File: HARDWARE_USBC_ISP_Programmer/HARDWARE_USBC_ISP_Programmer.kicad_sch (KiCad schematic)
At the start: 45 parts

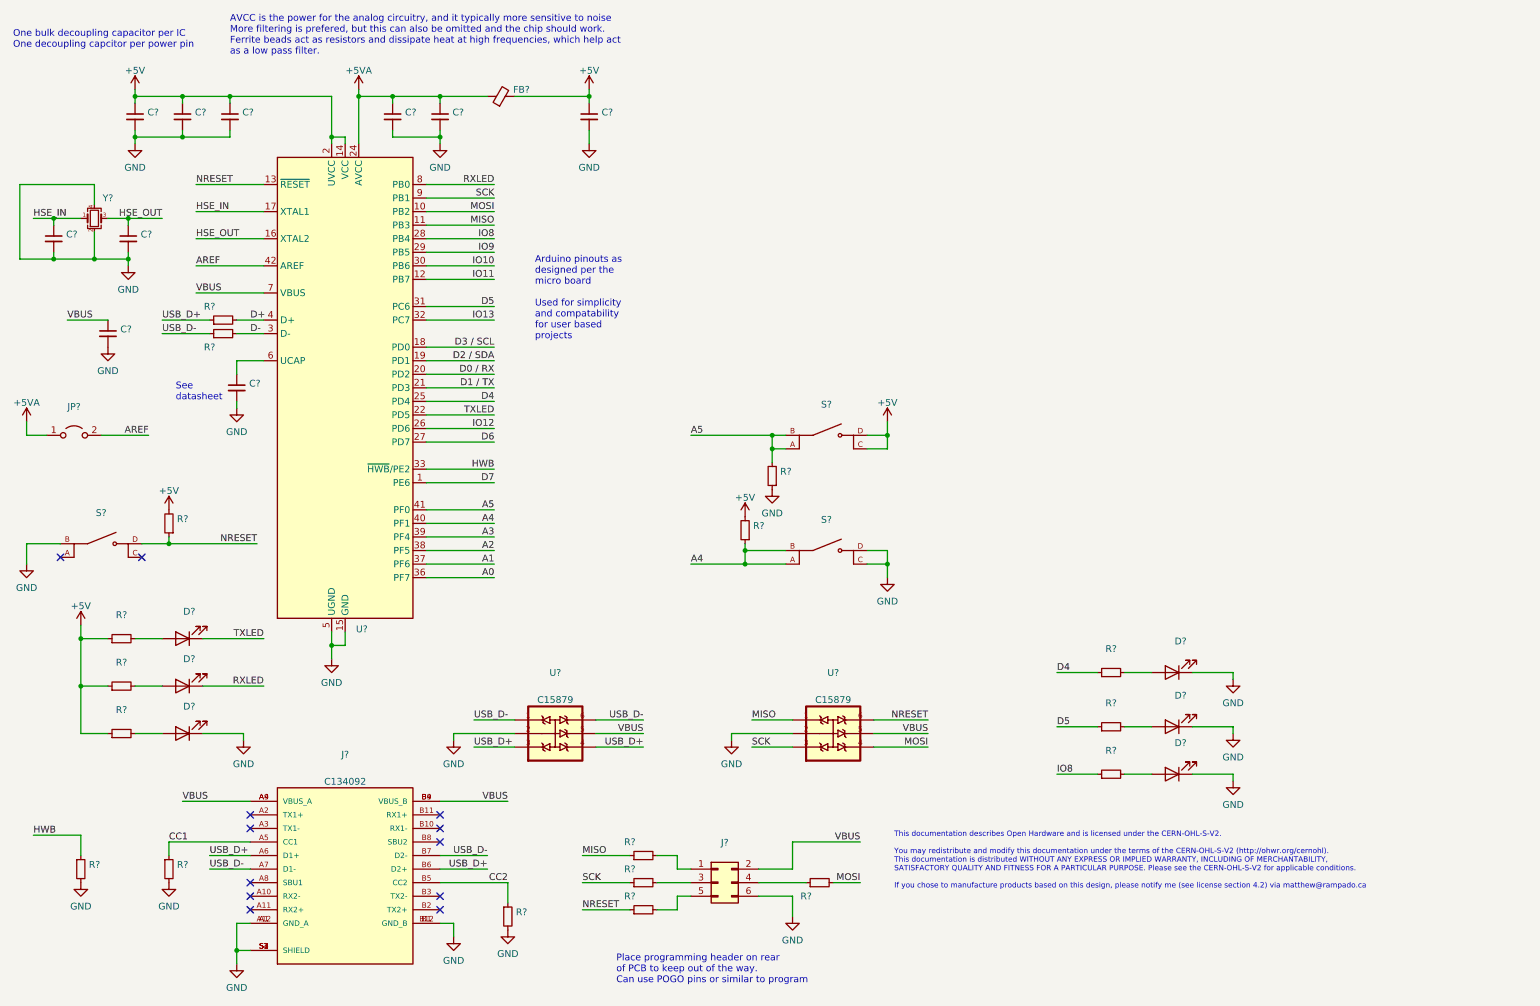
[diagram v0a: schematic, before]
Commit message: Added headers to schematic, other minor changes
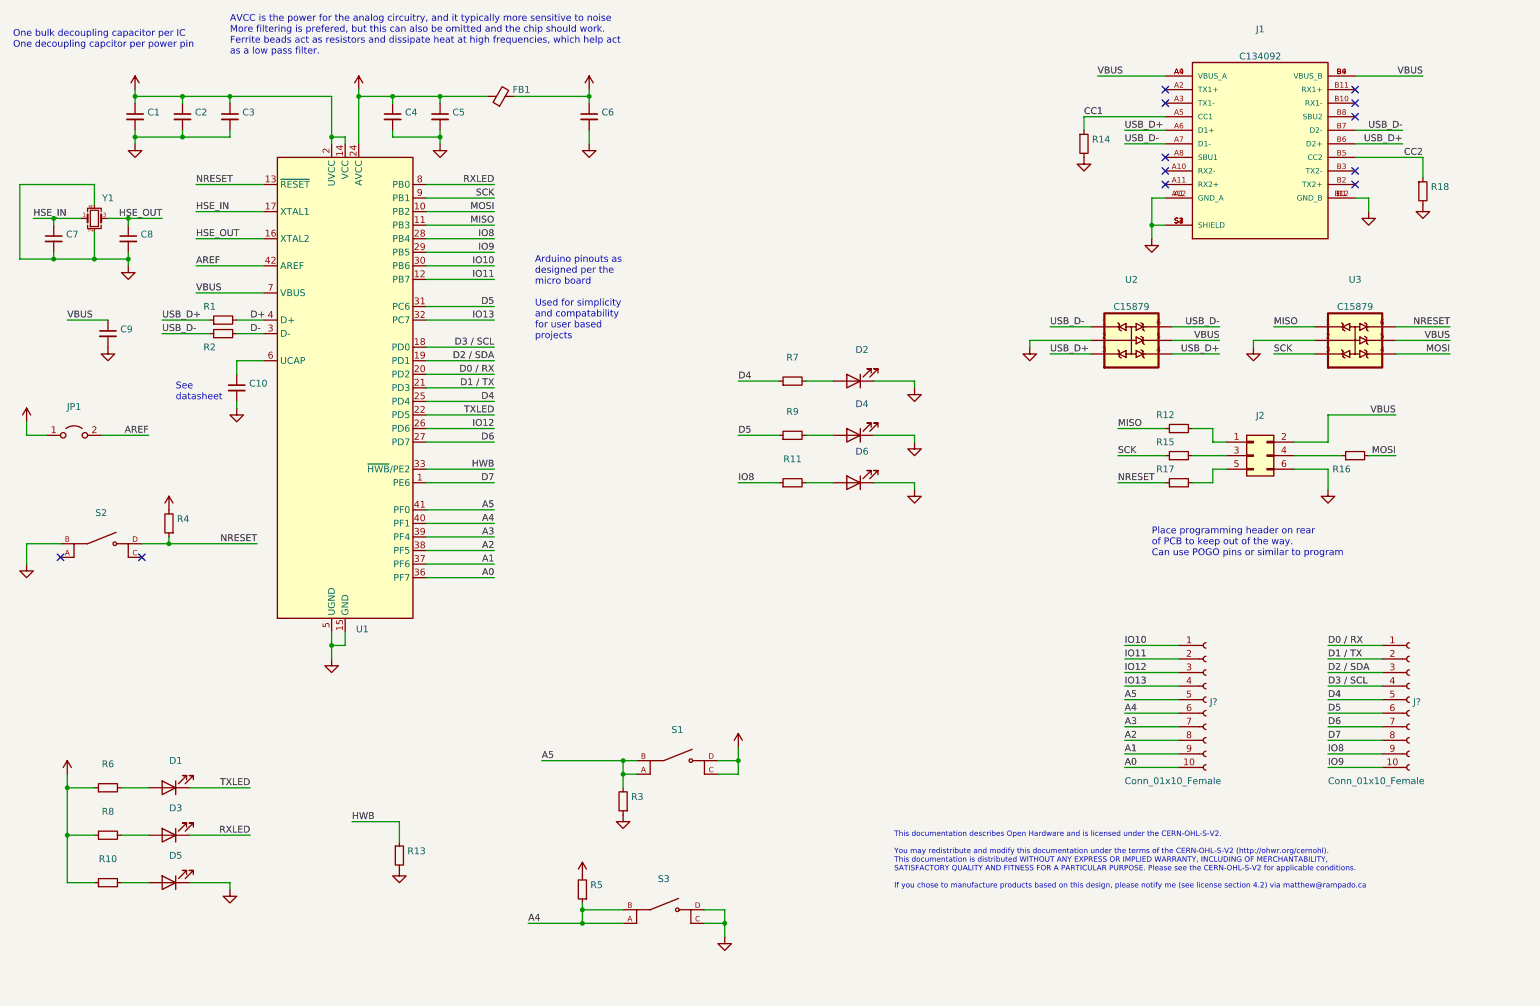
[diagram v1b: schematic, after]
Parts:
- added J? (x2): Conn_01x10_Female, symbol Connector:Conn_01x10_Female
- J1: renamed from J?; footprint (none) -> Rampado_Master:MOLEX_105450-0101
- S1, S2, S3: renamed from S?; footprint (none) -> Rampado_Master:SW_TS-1187A-B-A-B
- U2, U3: renamed from U?; footprint (none) -> Rampado_Master:SOT65P210X110-6N
- gave numbers to parts that had none: 39
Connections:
- net A0: now also J?.10 (Pin_10)
- net A1: now also J?.9 (Pin_9)
- net A2: now also J?.8 (Pin_8)
- net A3: now also J?.7 (Pin_7)
- net A4: now also J?.6 (Pin_6)
- net A5: now also J?.5 (Pin_5)
- net D0 / RX: now also J?.1 (Pin_1)
- net D1 / TX: now also J?.2 (Pin_2)
- net D2 / SDA: now also J?.3 (Pin_3)
- net D3 / SCL: now also J?.4 (Pin_4)
- net D4: now also J?.5 (Pin_5)
- net D5: now also J?.6 (Pin_6)
- net D6: now also J?.7 (Pin_7)
- net D7: now also J?.8 (Pin_8)
- net IO10: now also J?.1 (Pin_1)
- net IO11: now also J?.2 (Pin_2)
- net IO12: now also J?.3 (Pin_3)
- net IO13: now also J?.4 (Pin_4)
- net IO8: now also J?.9 (Pin_9)
- net IO9: now also J?.10 (Pin_10)
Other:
- moved on the sheet: D1, D2, D3, D4, D5, D6, J1, J2, R10, R11, R12, R13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

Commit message: Finalized footprints and schematic
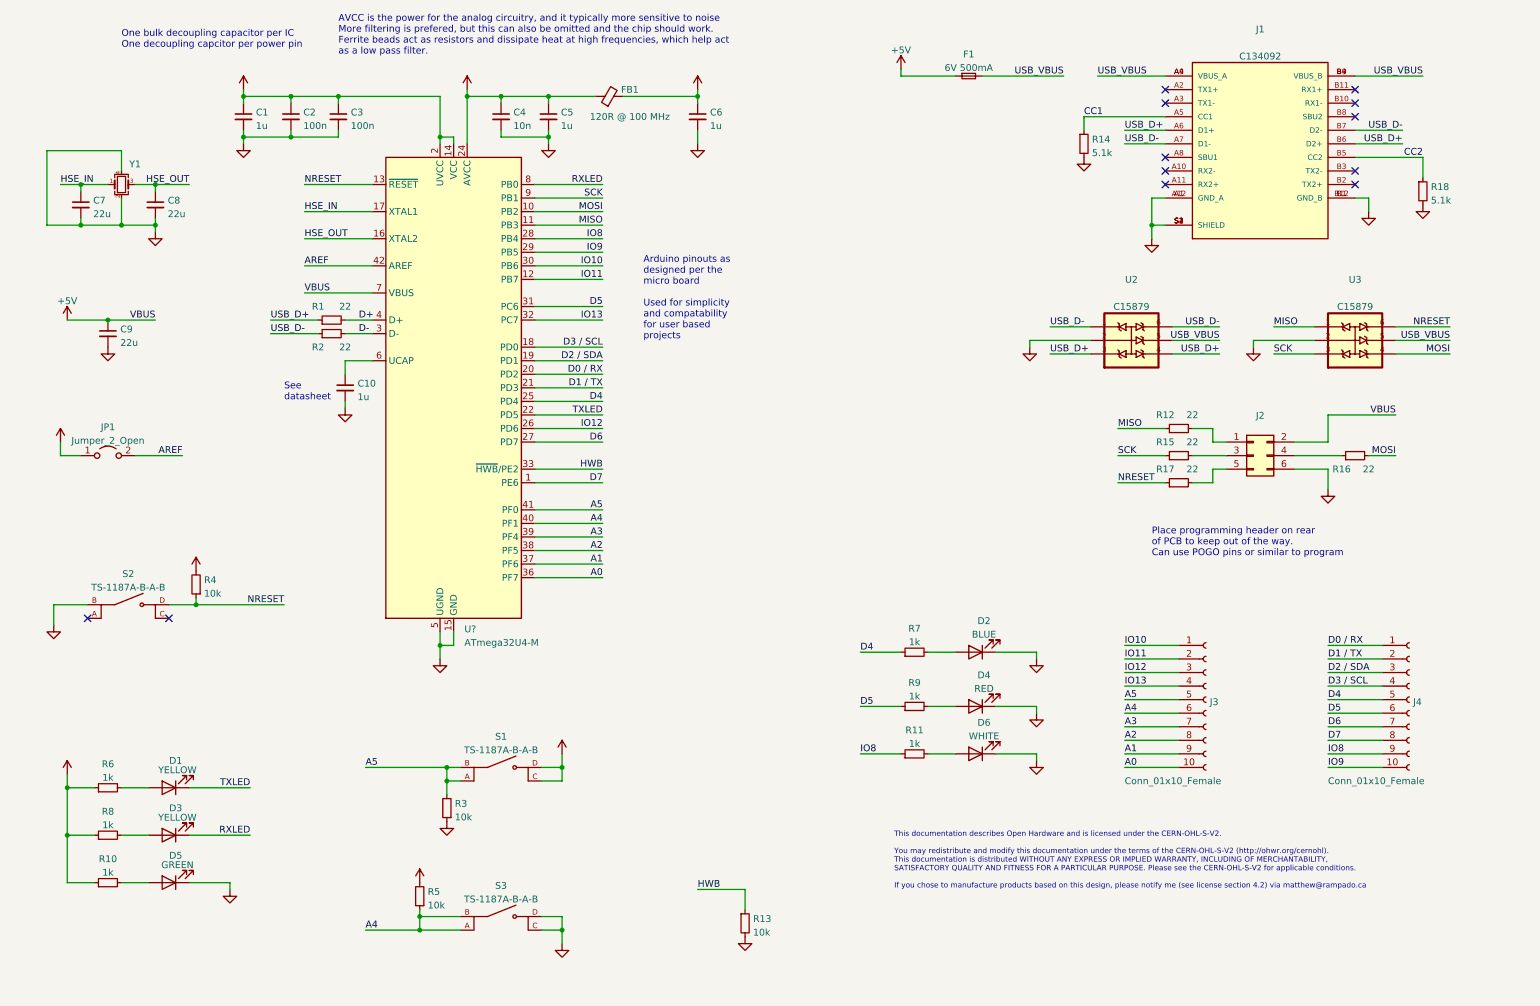
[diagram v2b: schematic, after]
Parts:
- removed U1: (no value), symbol MCU_Microchip_ATmega:ATmega32U4-M
- added F1: 6V 500mA, Fuse:Fuse_0603_1608Metric_Pad1.05x0.95mm_HandSolder, symbol Device:Fuse_Small
- added U?: ATmega32U4-M, Package_DFN_QFN:QFN-44-1EP_7x7mm_P0.5mm_EP5.2x5.2mm, symbol MCU_Microchip_ATmega:ATmega32U4-M
- C1, C10, C5, C6: value (none) -> 1u; footprint (none) -> Capacitor_SMD:C_0603_1608Metric
- C2, C3: value (none) -> 100n; footprint (none) -> Capacitor_SMD:C_0603_1608Metric
- C4: value (none) -> 10n; footprint (none) -> Capacitor_SMD:C_0603_1608Metric
- C7, C8, C9: value (none) -> 22u; footprint (none) -> Capacitor_SMD:C_0603_1608Metric
- D1, D3: value (none) -> YELLOW; footprint (none) -> LED_SMD:LED_0603_1608Metric
- D2: value (none) -> BLUE; footprint (none) -> LED_SMD:LED_0603_1608Metric
- D4: value (none) -> RED; footprint (none) -> LED_SMD:LED_0603_1608Metric
- D5: value (none) -> GREEN; footprint (none) -> LED_SMD:LED_0603_1608Metric
- D6: value (none) -> WHITE; footprint (none) -> LED_SMD:LED_0603_1608Metric
- FB1: value (none) -> 120R @ 100 MHz; footprint (none) -> Inductor_SMD:L_0603_1608Metric
- J2: footprint (none) -> Connector_PinHeader_2.54mm:PinHeader_2x03_P2.54mm_Vertical
- J3, J4: renamed from J?; footprint (none) -> Connector_PinSocket_2.54mm:PinSocket_1x10_P2.54mm_Vertical
- JP1: value (none) -> Jumper_2_Open; footprint (none) -> Jumper:SolderJumper-2_P1.3mm_Open_RoundedPad1.0x1.5mm
- R1, R12, R15, R16, R17, R2: value (none) -> 22; footprint (none) -> Resistor_SMD:R_0603_1608Metric
- R10, R11, R6, R7, R8, R9: value (none) -> 1k; footprint (none) -> Resistor_SMD:R_0603_1608Metric
- R13: value (none) -> 10k; footprint (none) -> Resistor_SMD:R_0603_1608Metric; JLCPCB Part # C23186 -> C25804
- R14, R18: value (none) -> 5.1k; footprint (none) -> Resistor_SMD:R_0603_1608Metric
- R3, R4, R5: value (none) -> 10k; footprint (none) -> Resistor_SMD:R_0603_1608Metric; JLCPCB Part # C21190 -> C25804
- S1, S2, S3: value (none) -> TS-1187A-B-A-B
- Y1: footprint (none) -> Crystal:Crystal_SMD_3225-4Pin_3.2x2.5mm
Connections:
- net +5V: now also C9.1, J2.2 (Pin_2), F1.1, U?.14 (VCC), U?.2 (UVCC), U?.34 (VCC), U?.7 (VBUS)
- net +5VA: now also U?.24 (AVCC), U?.44 (AVCC)
- net A0: now also U?.36 (PF7)
- net A1: now also U?.37 (PF6)
- net A2: now also U?.38 (PF5)
- net A3: now also U?.39 (PF4)
- net A4: now also U?.40 (PF1)
- net A5: now also U?.41 (PF0)
- net AREF: now also U?.42 (AREF)
- net D+: now also U?.4 (D+)
- net D-: now also U?.3 (D-)
- net D0 / RX: now also U?.20 (PD2)
- net D1 / TX: now also U?.21 (PD3)
- net D2 / SDA: now also U?.19 (PD1)
- net D3 / SCL: now also U?.18 (PD0)
- net D4: now also U?.25 (PD4)
- net D5: now also U?.31 (PC6)
- net D6: now also U?.27 (PD7)
- net D7: now also U?.1 (PE6)
- net GND: now also U?.15 (GND), U?.23 (GND), U?.35 (GND), U?.43 (GND), U?.45 (GND), U?.5 (UGND)
- net HSE_IN: now also U?.17 (XTAL1)
- net HSE_OUT: now also U?.16 (XTAL2)
- net HWB: now also U?.33 (~{HWB}/PE2)
- net IO10: now also U?.30 (PB6)
- net IO11: now also U?.12 (PB7)
- net IO12: now also U?.26 (PD6)
- net IO13: now also U?.32 (PC7)
- net IO8: now also U?.28 (PB4)
- net IO9: now also U?.29 (PB5)
- net MISO: now also U?.11 (PB3)
- net MOSI: now also U?.10 (PB2)
- net NRESET: now also U?.13 (~{RESET})
- net RXLED: now also U?.8 (PB0)
- net SCK: now also U?.9 (PB1)
- net TXLED: now also U?.22 (PD5)
- net at C10.1: now also U?.6 (UCAP)
- net VBUS renamed USB_VBUS
- net USB_VBUS: now also F1.2; no longer C9.1, J2.2 (Pin_2)
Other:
- moved on the sheet: C1, C10, C2, C3, C4, C5, C6, C7, C8, D2, D4, D6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

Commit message: Initial PCB layout complete
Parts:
- gave numbers to parts that had none: 1
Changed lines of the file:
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@@
   (symbol (lib_id "MCU_Microchip_ATmega:ATmega32U4-M") (at 95.25 83.82 0) (unit 1)
     (in_bom yes) (on_board yes) (fields_autoplaced)
-    (property "Reference" "U?" (id 0) (at 97.2694 129.0304 0)
+    (property "Reference" "U1" (id 0) (at 97.2694 129.0304 0)
       (effects (font (size 1.27 1.27)) (justify left))
     )
@@
       (reference "S3") (unit 1) (value "TS-1187A-B-A-B") (footprint "Rampado_Master:SW_TS-1187A-B-A-B")
     )
+    (path "/9f43d1c3-9884-48c3-9a0e-a3ae0b6b2875"
+      (reference "U1") (unit 1) (value "ATmega32U4-M") (footprint "Package_DFN_QFN:QFN-44-1EP_7x7mm_P0.5mm_EP5.2x5.2mm")
+    )
     (path "/9d4d08dc-598c-409d-8f88-24678d093d71"
       (reference "U2") (unit 1) (value "SMF05CT1G") (footprint "Rampado_Master:SOT65P210X110-6N")
@@
       (reference "U3") (unit 1) (value "SMF05CT1G") (footprint "Rampado_Master:SOT65P210X110-6N")
     )
-    (path "/9f43d1c3-9884-48c3-9a0e-a3ae0b6b2875"
-      (reference "U?") (unit 1) (value "ATmega32U4-M") (footprint "Package_DFN_QFN:QFN-44-1EP_7x7mm_P0.5mm_EP5.2x5.2mm")
-    )
     (path "/ad3562f5-456c-4345-9674-ab2e13f88574"

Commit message: V1 routing complete
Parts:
- J1: value (none) -> 105450-0101
- J2: value (none) -> Conn_02x03_Odd_Even
- U2, U3: value (none) -> SMF05CT1G
- Y1: value (none) -> 16MHz
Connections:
- net +5V: now also U3.5
- net USB_VBUS: no longer U3.5
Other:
- moved on the sheet: U2, U3

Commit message: Created manufacturing files and prepare for review
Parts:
- FB1: footprint Inductor_SMD:L_0603_1608Metric -> Inductor_SMD:L_0805_2012Metric
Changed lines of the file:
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@@
   (symbol (lib_id "power:+5V") (at 274.32 73.66 0) (unit 1)
     (in_bom yes) (on_board yes) (fields_autoplaced)
-    (property "Reference" "#PWR?" (id 0) (at 274.32 77.47 0)
+    (property "Reference" "#PWR0102" (id 0) (at 274.32 77.47 0)
       (effects (font (size 1.27 1.27)) hide)
     )
@@
     (property "Reference" "FB1" (id 0) (at 128.27 27.94 90))
     (property "Value" "120R @ 100 MHz" (id 1) (at 128.27 33.02 90))
-    (property "Footprint" "Inductor_SMD:L_0603_1608Metric" (id 2) (at 124.46 30.988 90)
+    (property "Footprint" "Inductor_SMD:L_0805_2012Metric" (id 2) (at 124.46 30.988 90)
       (effects (font (size 1.27 1.27)) hide)
     )
@@
     )
     (path "/36461b23-f731-4bcd-862d-02ad30c87a33"
-      (reference "#PWR?") (unit 1) (value "+5V") (footprint "")
+      (reference "#PWR0102") (unit 1) (value "+5V") (footprint "")
     )
     (path "/ddf7157e-35ef-40c5-adc3-10269d86220e"
@@
     )
     (path "/b4d7bb65-5ec4-4633-b516-28ce90b29a9d"
-      (reference "FB1") (unit 1) (value "120R @ 100 MHz") (footprint "Inductor_SMD:L_0603_1608Metric")
+      (reference "FB1") (unit 1) (value "120R @ 100 MHz") (footprint "Inductor_SMD:L_0805_2012Metric")
     )
     (path "/94c518cf-8c9d-41a5-8f6f-52dc710eba1d"

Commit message: More changes
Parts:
- C7, C8: value 22u -> 22p
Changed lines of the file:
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@@
       (effects (font (size 1.27 1.27)) (justify left))
     )
-    (property "Value" "22u" (id 1) (at 27.7241 51.2385 0)
+    (property "Value" "22p" (id 1) (at 27.7241 51.2385 0)
       (effects (font (size 1.27 1.27)) (justify left))
     )
@@
       (effects (font (size 1.27 1.27)) (justify left))
     )
-    (property "Value" "22u" (id 1) (at 41.6941 51.2385 0)
+    (property "Value" "22p" (id 1) (at 41.6941 51.2385 0)
       (effects (font (size 1.27 1.27)) (justify left))
     )
@@
     )
     (path "/5c4c6144-ba0d-4bd9-aee2-e83ba07dbb07"
-      (reference "C7") (unit 1) (value "22u") (footprint "Capacitor_SMD:C_0603_1608Metric")
+      (reference "C7") (unit 1) (value "22p") (footprint "Capacitor_SMD:C_0603_1608Metric")
     )
     (path "/68edd251-1b11-46f8-ab47-8b2e7e1e96bb"
-      (reference "C8") (unit 1) (value "22u") (footprint "Capacitor_SMD:C_0603_1608Metric")
+      (reference "C8") (unit 1) (value "22p") (footprint "Capacitor_SMD:C_0603_1608Metric")
     )
     (path "/19838642-ec96-4b78-9eaa-f72cf2f34bfb"
